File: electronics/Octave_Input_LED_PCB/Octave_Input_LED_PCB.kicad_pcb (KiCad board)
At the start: 2 copper layers, 106.8 x 57.2 mm, 61 parts, among them J1 HRO_TYPE-C-31-M-12, J2 Conn_01x12, J3 Conn_01x12, SW1 SW_Hot_Swap_Socket, SW10 SW_Hot_Swap_Socket, SW11 SW_Hot_Swap_Socket, SW12 SW_Hot_Swap_Socket, SW2 SW_Hot_Swap_Socket, SW21 Alps_Alpine_SKRP, SW22 Alps_Alpine_SKRP, SW3 SW_Hot_Swap_Socket, SW4 SW_Hot_Swap_Socket, SW5 SW_Hot_Swap_Socket, SW6 SW_Hot_Swap_Socket, SW7 SW_Hot_Swap_Socket, SW8 SW_Hot_Swap_Socket, SW9 SW_Hot_Swap_Socket, U1 AP2112K-3.3, U2 Raspberry_Pi_RP2040, U3 W25Q64JVSS, Y1 12MHz

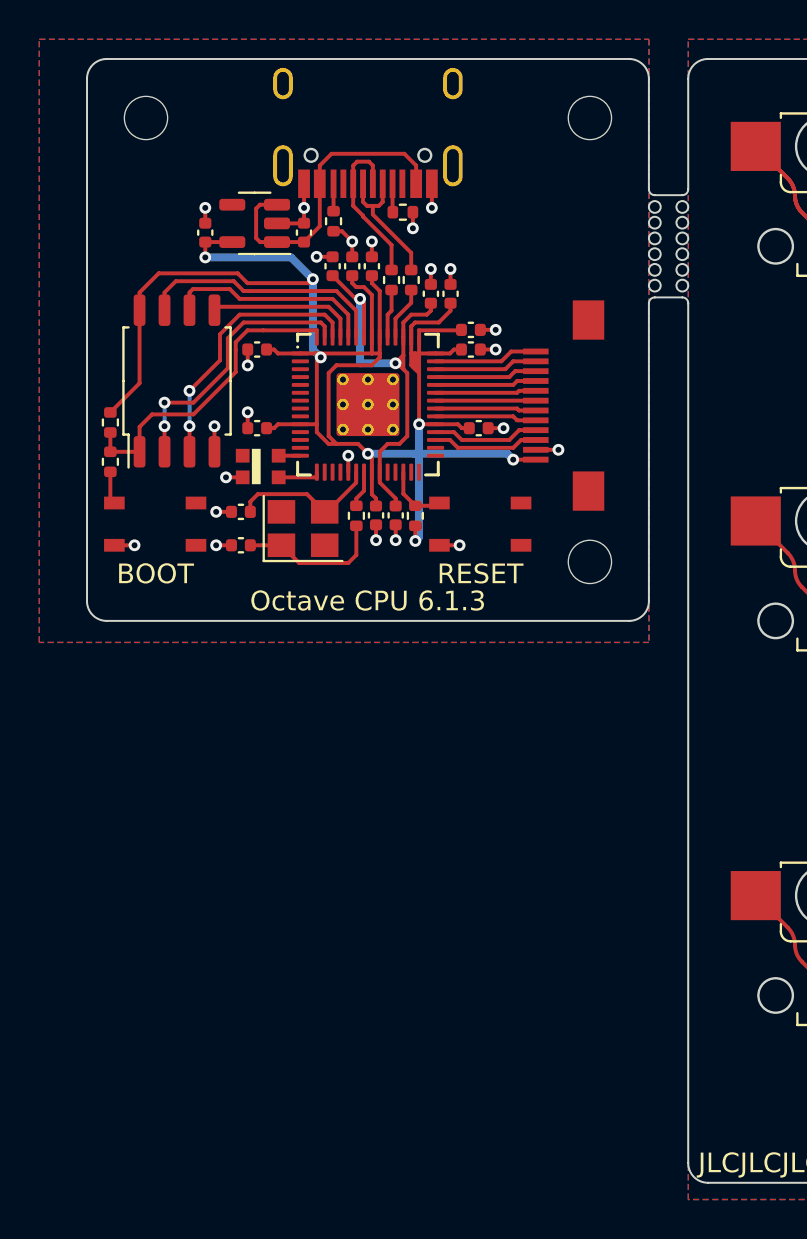
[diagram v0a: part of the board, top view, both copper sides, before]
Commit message: Remove CPU PCB from Input LED PCB
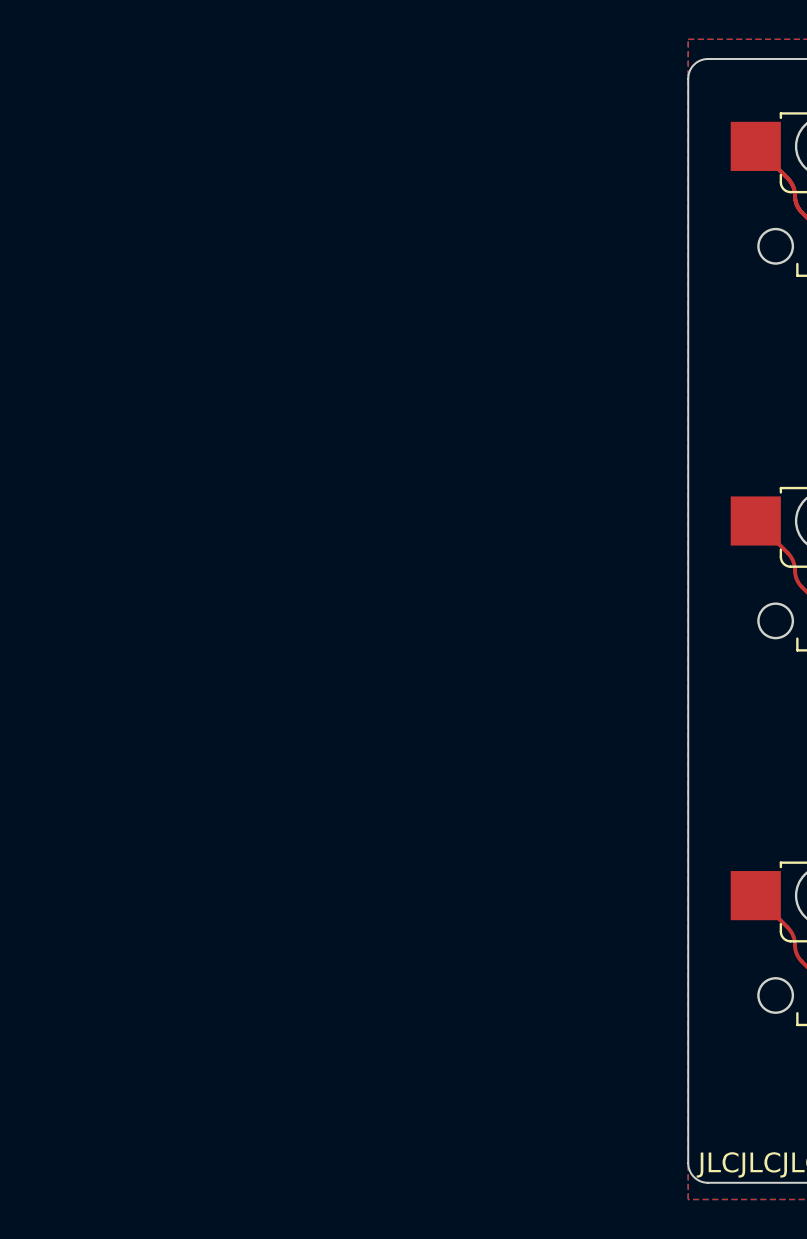
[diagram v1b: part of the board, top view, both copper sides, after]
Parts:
- removed C1, C2: 10uF, Capacitor_SMD:C_0402_1005Metric
- removed C10, C11, C12, C13, C14, C5, C6, C7, C8, C9: 0.1uF, Capacitor_SMD:C_0402_1005Metric
- removed C15, C16: 30pF, Capacitor_SMD:C_0402_1005Metric
- removed C3, C4: 1uF, Capacitor_SMD:C_0402_1005Metric
- removed J1: HRO_TYPE-C-31-M-12, Octave_Library:HRO_TYPE-C-31-M-12
- removed J2: Conn_01x12, Octave_Library:JUSHUO_AFC01-S12FCC-00
- removed LED1: WS2812C-2020-V1, Octave_Library:WS2812C-2020
- removed R1, R2: 5.1K, Resistor_SMD:R_0402_1005Metric
- removed R3, R4: 27, Resistor_SMD:R_0402_1005Metric
- removed R5, R6: 10K, Resistor_SMD:R_0402_1005Metric
- removed R7, R8: 1K, Resistor_SMD:R_0402_1005Metric
- removed REF** (x3): MountingHole_2.2mm_M2, MountingHole:MountingHole_2.2mm_M2
- removed SW21, SW22: Alps_Alpine_SKRP, Octave_Library:Tactile_Switch_SKRP_Series
- removed U1: AP2112K-3.3, Package_TO_SOT_SMD:SOT-23-5
- removed U2: Raspberry_Pi_RP2040, Octave_Library:RP2040_QFN-56
- removed U3: W25Q64JVSS, Package_SO:SOIC-8_5.23x5.23mm_P1.27mm
- removed Y1: 12MHz, Crystal:Crystal_SMD_3225-4Pin_3.2x2.5mm
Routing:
- net +3V3: track 97.4 -> 0.00 mm, vias 7 -> 0
- net GND: track 24.6 -> 0.00 mm, vias 24 -> 0
- net +1V1: track 23.3 -> 0.00 mm, vias 2 -> 0
- net +5V: track 15.7 -> 0.00 mm
- net QSPI_SS_N: track 15.7 -> 0.00 mm
- net QSPI_SD1: track 13.8 -> 0.00 mm, vias 2 -> 0
- net QSPI_SD2: track 13.7 -> 0.00 mm, vias 2 -> 0
- net QSPI_SD3: track 12.8 -> 0.00 mm
- net QSPI_SCLK: track 10.7 -> 0.00 mm
- net Net-(J1-PadA6): track 8.21 -> 0.00 mm
- net QSPI_SD0: track 7.66 -> 0.00 mm
- net Net-(C15-Pad1): track 7.46 -> 0.00 mm
- net Net-(C16-Pad1): track 7.41 -> 0.00 mm
- net Net-(J1-PadA7): track 7.08 -> 0.00 mm
- net IO1_MPU: track 5.47 -> 0.00 mm
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- removed copper zone on F.Cu, net +3V3
- removed copper zone on B.Cu, net GND
- removed copper zone on F.Cu, net GND
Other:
- board size 106.8 x 57.2 mm -> 76.2 x 57.2 mm
- board text removed: "BOOT"
- board text removed: "Octave CPU 6.1.3"
- board text removed: "RESET"

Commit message: Add footprint of WS2812B-Mini with inverted placement
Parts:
- added LED201: WS2812B-Mini V3, Octave_Library:WS2812B-Mini_Inverted, F.Cu at (133.7, 45.5)
- added LED202: WS2812B-Mini V3, Octave_Library:WS2812B-Mini_Inverted, F.Cu at (114.6, 45.5)
- added LED203: WS2812B-Mini V3, Octave_Library:WS2812B-Mini_Inverted, F.Cu at (95.6, 45.5)
- added LED204: WS2812B-Mini V3, Octave_Library:WS2812B-Mini_Inverted, F.Cu at (76.5, 45.5)
- added LED205: WS2812B-Mini V3, Octave_Library:WS2812B-Mini_Inverted, F.Cu at (133.7, 64.6)
- added LED206: WS2812B-Mini V3, Octave_Library:WS2812B-Mini_Inverted, F.Cu at (114.6, 64.6)
- added LED207: WS2812B-Mini V3, Octave_Library:WS2812B-Mini_Inverted, F.Cu at (95.6, 64.6)
- added LED208: WS2812B-Mini V3, Octave_Library:WS2812B-Mini_Inverted, F.Cu at (76.5, 64.6)
- added LED209: WS2812B-Mini V3, Octave_Library:WS2812B-Mini_Inverted, F.Cu at (133.7, 83.6)
- added LED210: WS2812B-Mini V3, Octave_Library:WS2812B-Mini_Inverted, F.Cu at (114.6, 83.6)
- added LED211: WS2812B-Mini V3, Octave_Library:WS2812B-Mini_Inverted, F.Cu at (95.6, 83.6)
- added LED212: WS2812B-Mini V3, Octave_Library:WS2812B-Mini_Inverted, F.Cu at (76.5, 83.6)
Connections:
- J3 pad 1: unconnected-(J3-Pad1) -> +3V3
- J3 pad 2: unconnected-(J3-Pad2) -> GND
- J3 pad 3: unconnected-(J3-Pad3) -> IO0_MPU

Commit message: Improve edge cuts of WS2812B-Mini (Inverted)
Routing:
- net ROW0_UI: track 92.5 -> 68.9 mm
- net ROW1_UI: track 69.4 -> 49.6 mm
- net ROW2_UI: track 75.3 -> 55.6 mm

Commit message: Route PCB
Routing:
- net +3V3: track 0.00 -> 246.9 mm, vias 0 -> 7
- net Net-(LED204-Pad2): track 0.00 -> 88.5 mm, vias 0 -> 2
- net Net-(LED208-Pad2): track 0.00 -> 88.3 mm, vias 0 -> 2
- net IO0_MPU: track 0.00 -> 58.2 mm, vias 0 -> 2
- net GND: track 0.00 -> 20.8 mm, vias 0 -> 20
- net ROW0_UI: track 68.9 -> 87.8 mm, vias 2 -> 4
- net ROW1_UI: track 49.6 -> 68.6 mm, vias 0 -> 2
- net ROW2_UI: track 55.6 -> 72.9 mm
- net Net-(LED209-Pad2): track 0.00 -> 14.3 mm
- net Net-(LED205-Pad2): track 0.00 -> 14.3 mm
- net Net-(LED201-Pad2): track 0.00 -> 14.3 mm
- net Net-(LED211-Pad2): track 0.00 -> 14.3 mm
- net Net-(LED210-Pad2): track 0.00 -> 14.3 mm
- net Net-(LED207-Pad2): track 0.00 -> 14.3 mm
- net Net-(LED206-Pad2): track 0.00 -> 14.3 mm
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- added copper zone on B.Cu, net GND
- added copper zone on F.Cu, net GND
- removed copper zone on B.Cu, net (none)
- removed copper zone on F.Cu, net (none)

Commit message: Update Octave_Input_LED_PCB.kicad_pcb
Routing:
- net Net-(LED208-Pad2): track 88.3 -> 106.7 mm
- net +3V3: track 246.9 -> 239.3 mm
- net Net-(LED204-Pad2): track 88.5 -> 87.0 mm
- net COL0_UI: track 77.9 -> 76.6 mm
- net IO0_MPU: track 58.2 -> 58.9 mm
- net GND: track 20.8 -> 20.1 mm, vias 20 -> 13
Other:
- board text added: "Octave Input LED 1.0.0"
- board text removed: "Octave Input LED 0.0.0"
